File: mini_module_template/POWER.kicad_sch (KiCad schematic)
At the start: 27 parts, among them Q2 AO3400A, U4 AZ1117-3.3, U5 TPS563200

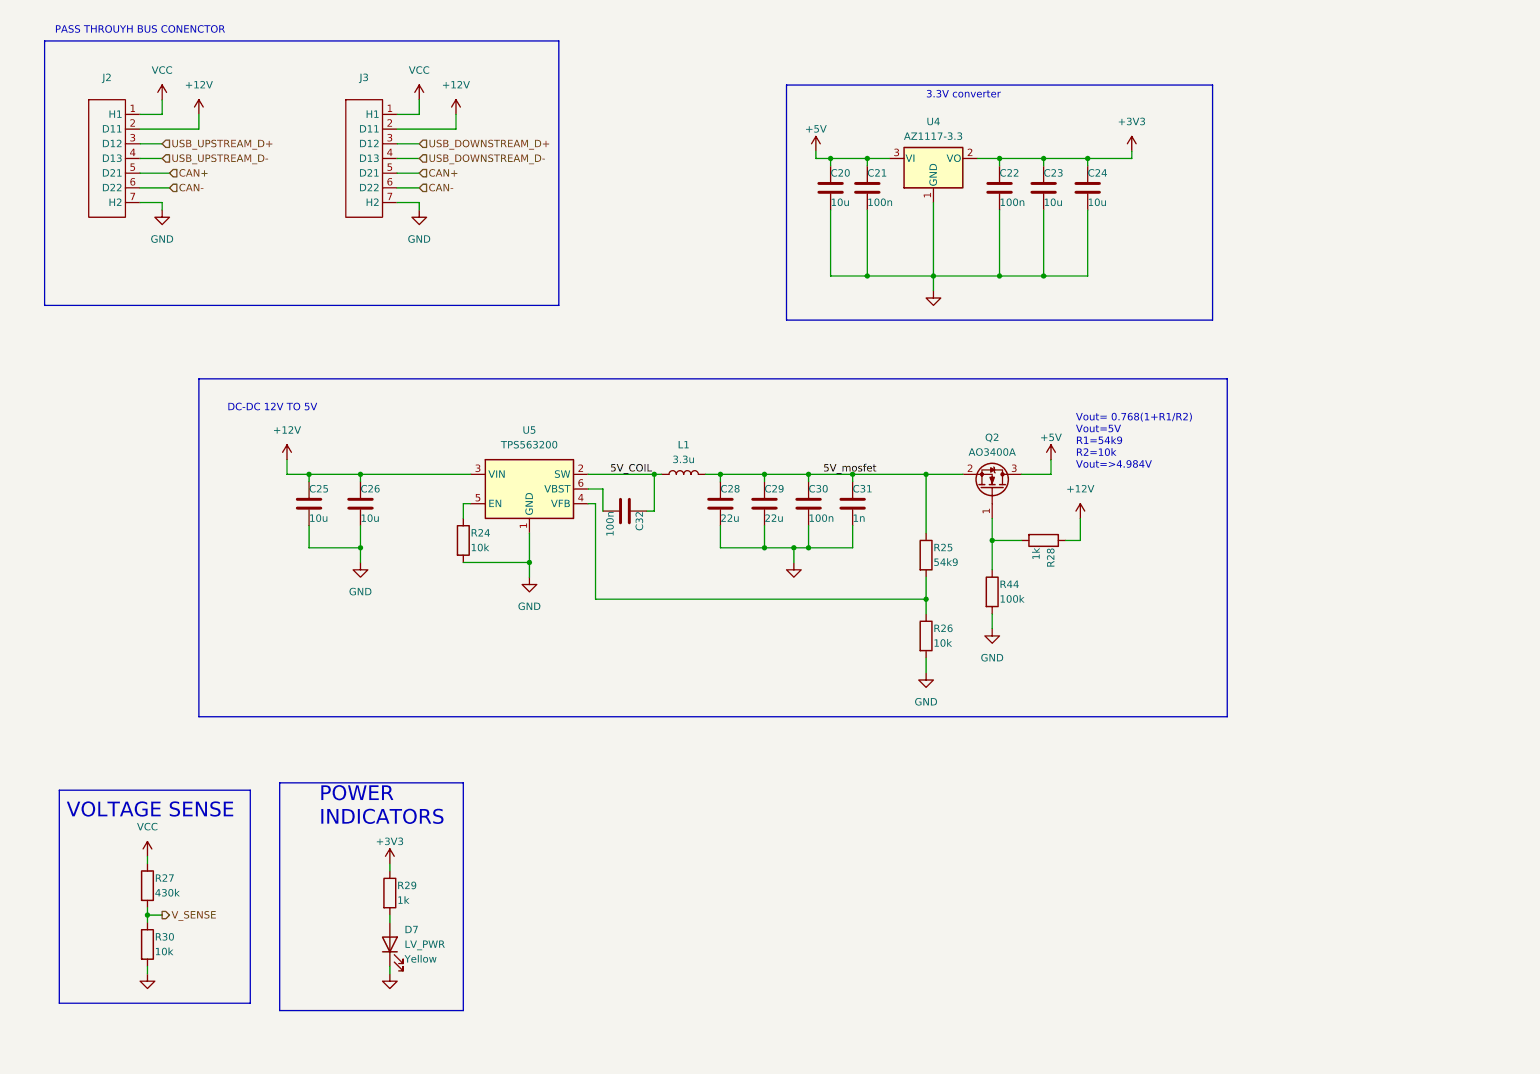
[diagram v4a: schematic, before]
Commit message: revison C, aded 2 can support and gight voltage input stepdown
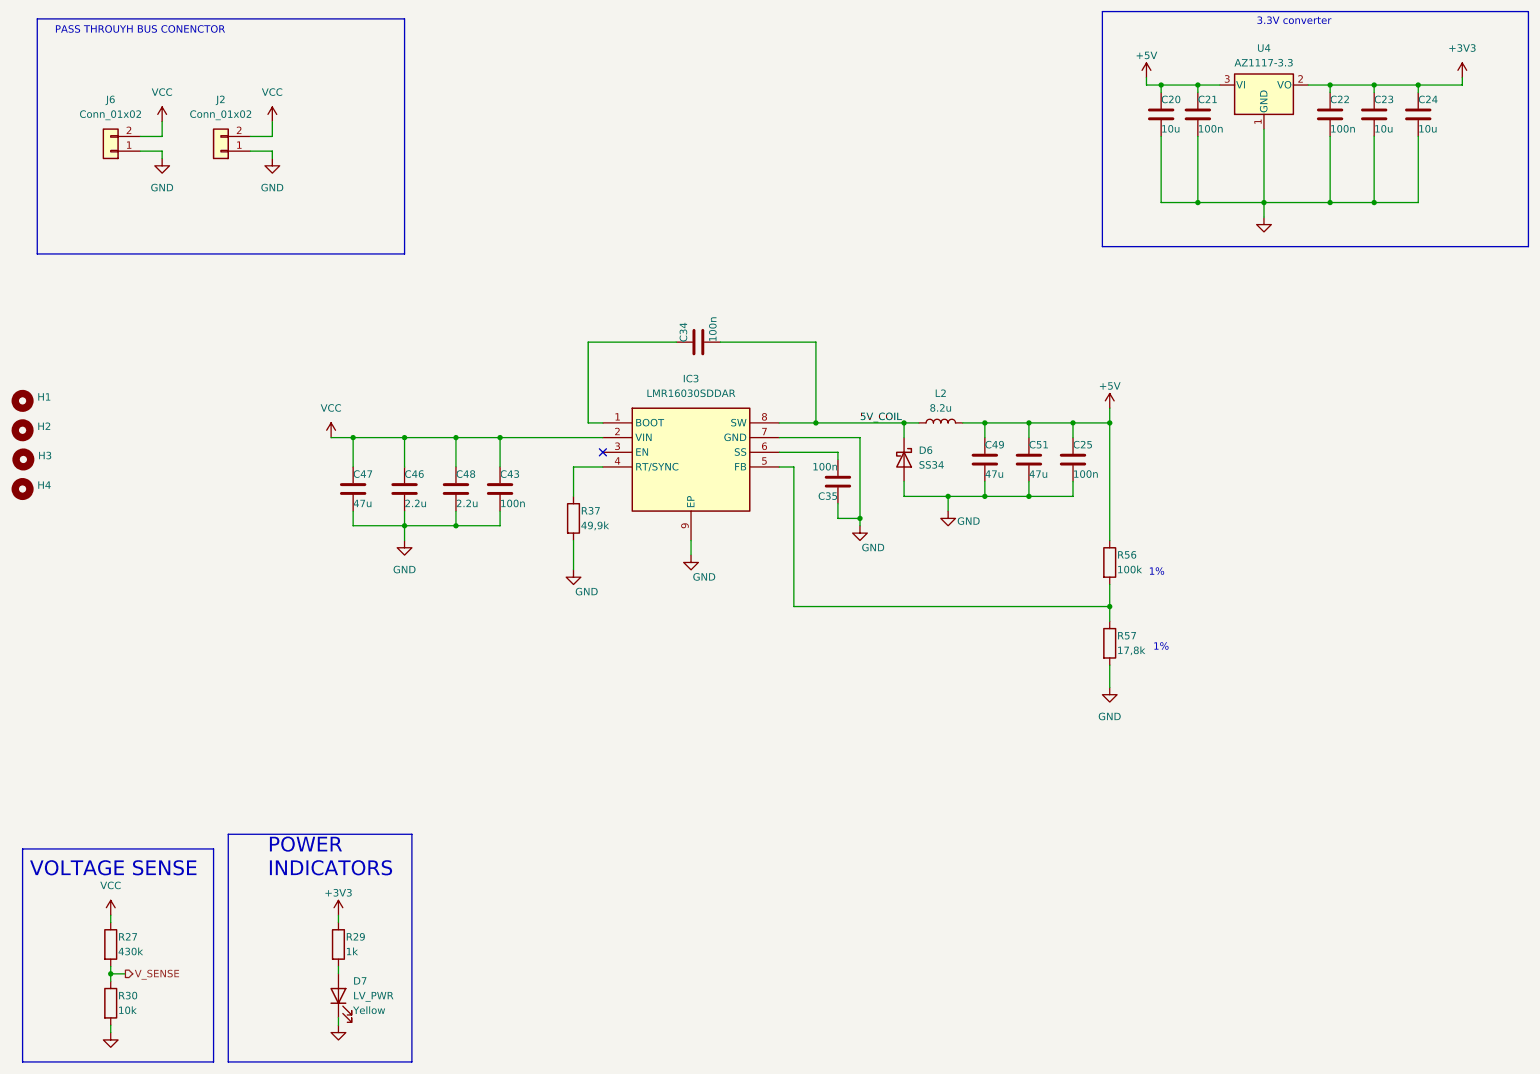
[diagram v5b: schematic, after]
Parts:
- removed C26: 10u, Capacitor_SMD:C_0805_2012Metric, symbol Device:C
- removed C28, C29: 22u, Capacitor_SMD:C_0805_2012Metric, symbol Device:C
- removed C30: 100n, Capacitor_SMD:C_0603_1608Metric, symbol Device:C
- removed C31: 1n, Capacitor_SMD:C_0603_1608Metric, symbol Device:C
- removed C32: 100n, Capacitor_SMD:C_0402_1005Metric, symbol Device:C
- removed J2, J3: ~, parts:DSUB-7w2, symbol DSUB_7w2:DSUB-7w2
- removed L1: 3.3u, Inductor_SMD:L_Changjiang_FNR4030S, symbol Device:L
- removed Q2: AO3400A, Package_TO_SOT_SMD:SOT-23, symbol Transistor_FET:AO3400A
- removed R24, R26: 10k, Resistor_SMD:R_0402_1005Metric, symbol Device:R
- removed R25: 54k9, Resistor_SMD:R_0402_1005Metric, symbol Device:R
- removed R28: 1k, Resistor_SMD:R_0402_1005Metric, symbol Device:R
- removed R44: 100k, Resistor_SMD:R_0402_1005Metric, symbol Device:R
- removed U5: TPS563200, Package_TO_SOT_SMD:SOT-23-6, symbol Regulator_Switching:TPS563200
- added C34, C35, C43: 100n, Capacitor_SMD:C_0402_1005Metric, symbol Device:C
- added C46, C48: 2.2u, Capacitor_SMD:C_1206_3216Metric, symbol Device:C
- added C47: 47u, Capacitor_SMD:C_Elec_10x10.2, symbol Device:C
- added C49, C51: 47u, Capacitor_SMD:C_1206_3216Metric, symbol Device:C
- added D6: SS34, Diode_SMD:D_SMA, symbol Diode:SS34
- added H1, H2, H3, H4: ~, MountingHole:MountingHole_3.2mm_M3, symbol Mechanical:MountingHole
- added IC3: LMR16030SDDAR, parts:SOIC127P600X170-9N, symbol LMR16030SDDAR:LMR16030SDDAR
- added J2, J6: Conn_01x02, Connector_AMASS:AMASS_XT60PW-M_1x02_P7.20mm_Horizontal, symbol Connector_Generic:Conn_01x02
- added L2: 8.2u, Inductor_SMD:L_Cenker_CKCS6045, symbol Device:L
- added R37: 49,9k, Resistor_SMD:R_0402_1005Metric, symbol Device:R
- added R56: 100k, Resistor_SMD:R_0402_1005Metric, symbol Device:R
- added R57: 17,8k, Resistor_SMD:R_0402_1005Metric, symbol Device:R
- C21: footprint Capacitor_SMD:C_0603_1608Metric -> Capacitor_SMD:C_0402_1005Metric
- C25: value 10u -> 100n; footprint Capacitor_SMD:C_0805_2012Metric -> Capacitor_SMD:C_0402_1005Metric
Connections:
- net +12V is gone; now on net +5V: C25.1
- net +5V: now also C49.1, C51.1, L2.2, R56.1
- net 5V_COIL: now also C34.2, D6.1 (K), IC3.8 (SW), L2.1
- net GND: now also C35.1, C43.2, C46.2, C47.2, C48.2, C49.2, C51.2, D6.2 (A), IC3.7 (GND), IC3.9 (EP), J2.1 (Pin_1), J6.1 (Pin_1), R37.2, R57.2
- net VCC: now also C43.1, C46.1, C47.1, C48.1, IC3.2 (VIN), J2.2 (Pin_2), J6.2 (Pin_2)
- new net: IC3.5 (FB), R56.2, R57.1
- new net: C35.2, IC3.6 (SS)
- new net: C34.1, IC3.1 (BOOT)
- new net: IC3.4 (RT/SYNC), R37.1
- no-connect marks 0 -> 1
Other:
- note added: "1%"
- note removed: "DC-DC 12V TO 5V"
- note removed: "Vout= 0.768(1+R1/R2) Vout=5V R1=54k9 R2=10k Vout=>4.984V"
- moved on the sheet: C20, C21, C22, C23, C24, D7, R27, R29, R30, U4

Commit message: final check rev A
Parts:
- R27: value 430k -> 43k; footprint Resistor_SMD:R_0603_1608Metric -> Resistor_SMD:R_0402_1005Metric
- R29: value 1k -> 220
- R30: value 10k -> 1k; footprint Resistor_SMD:R_0603_1608Metric -> Resistor_SMD:R_0402_1005Metric
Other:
- moved on the sheet: C20, C21, C22, C23, C24, D7, J2, J6, R27, R29, R30, U4

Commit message: updaet schematic
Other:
- company: (none) -> Patryk Dudziński
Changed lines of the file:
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@@
 	(title_block
 		(title "POWER DC to DC")
+		(date "2025-01-10")
+		(rev "1.0")
+		(company "Patryk Dudziński")
 	)
 	(junction
@@
 	(label "5V_COIL"
 		(at 165.1 85.09 0)
-		(fields_autoplaced yes)
 		(effects
 			(font
@@
 		(shape output)
 		(at 38.1 161.29 0)
-		(fields_autoplaced yes)
 		(effects
 			(font
